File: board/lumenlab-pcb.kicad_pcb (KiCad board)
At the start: 2 copper layers, 72 parts, among them J1 2.1mm Barrel Jack, J2 Screw_Terminal_01x04, J3 Screw_Terminal_01x06, J4 JTAG, SW1 SW_SPST, U1 MP2338, U2 AP7361C-33E, U3 SN74AHCT1G125, U4 SN74HC14DR, U5 ESP32-WROOM-32E, U6 1_Custom_LM386MX-1_NOPB

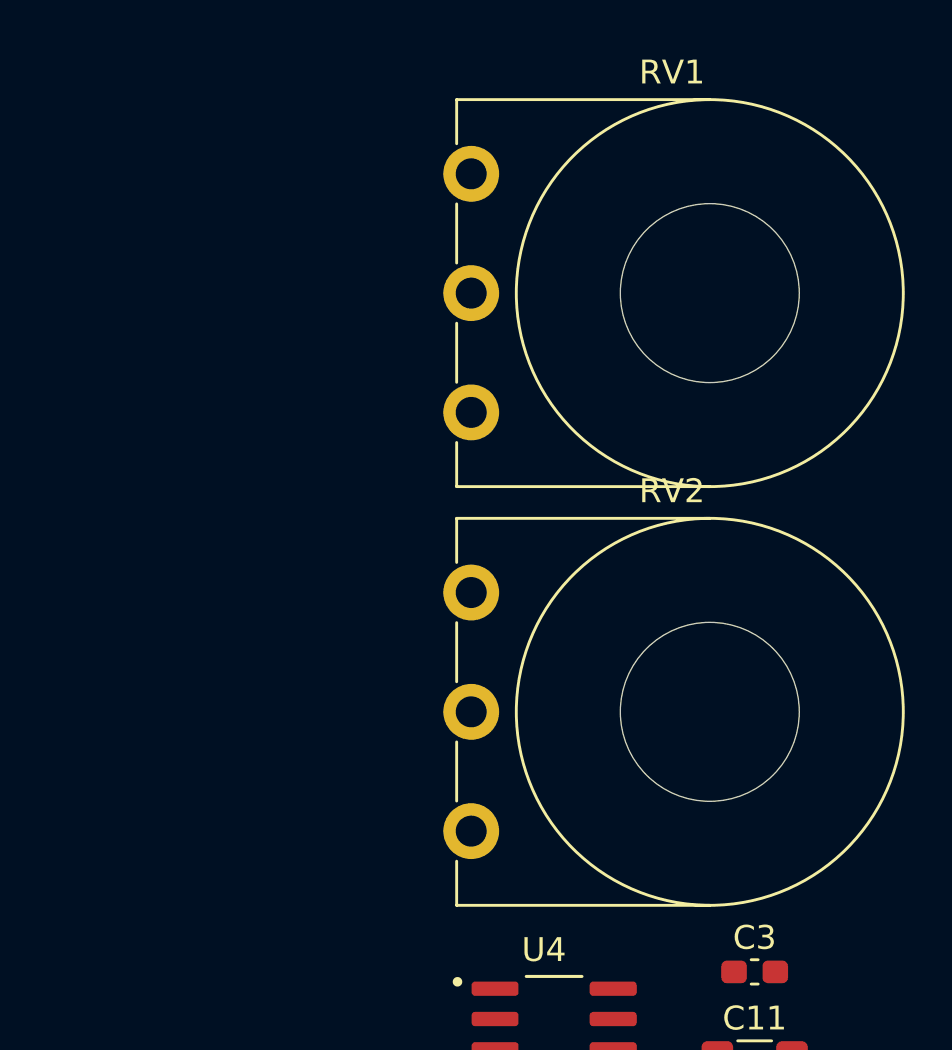
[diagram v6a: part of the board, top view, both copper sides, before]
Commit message: Footprint changes for package sizes and BOM additions
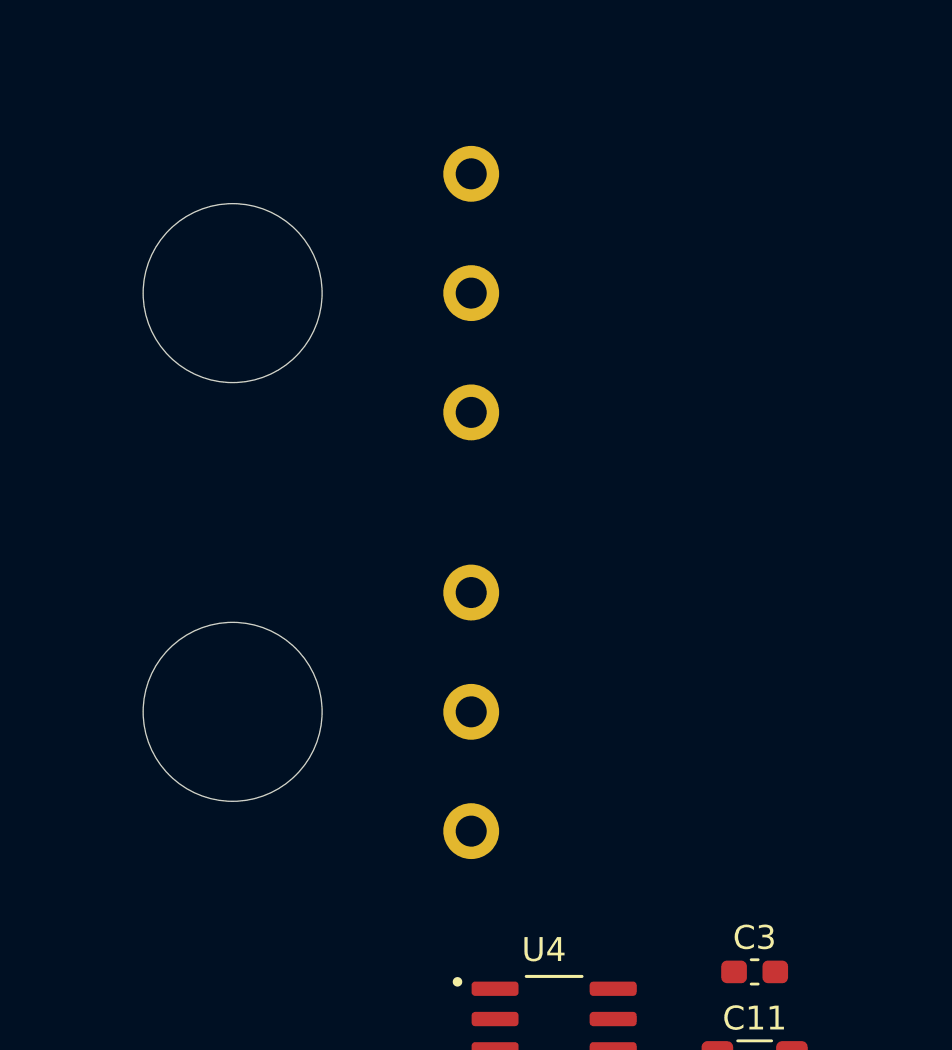
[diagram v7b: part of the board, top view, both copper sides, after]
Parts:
- RV1, RV2: moved to B.Cu
- U6: value 1_Custom_LM386MX-1_NOPB -> LM386MX
- turned RV1 to 180 degrees
- turned RV2 to 180 degrees

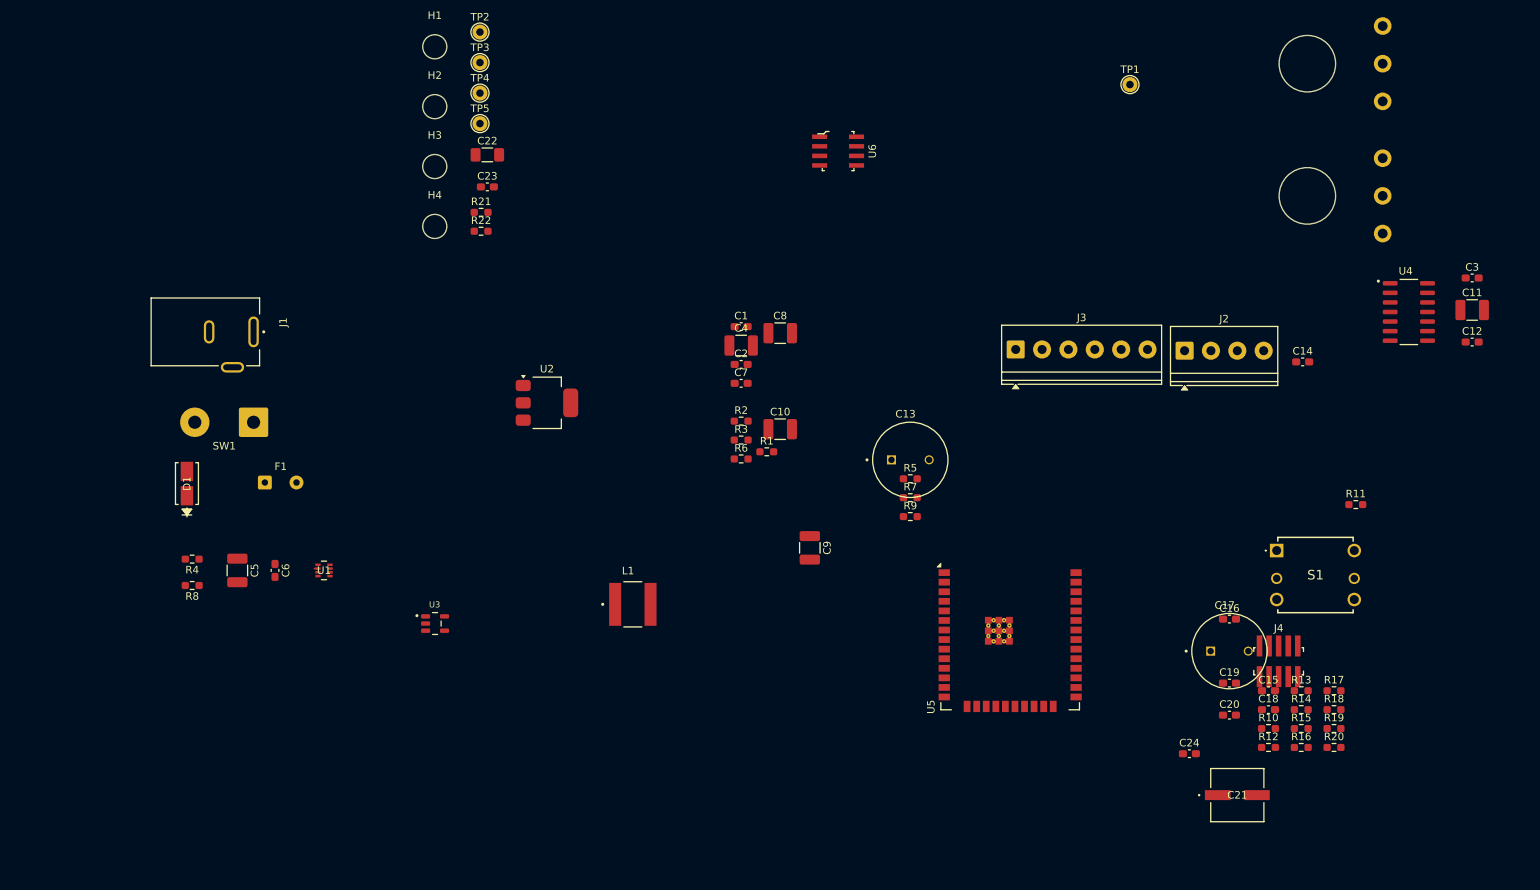
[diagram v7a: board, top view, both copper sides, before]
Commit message: Finalize schematic, footprint assignments, DigiKey BOM
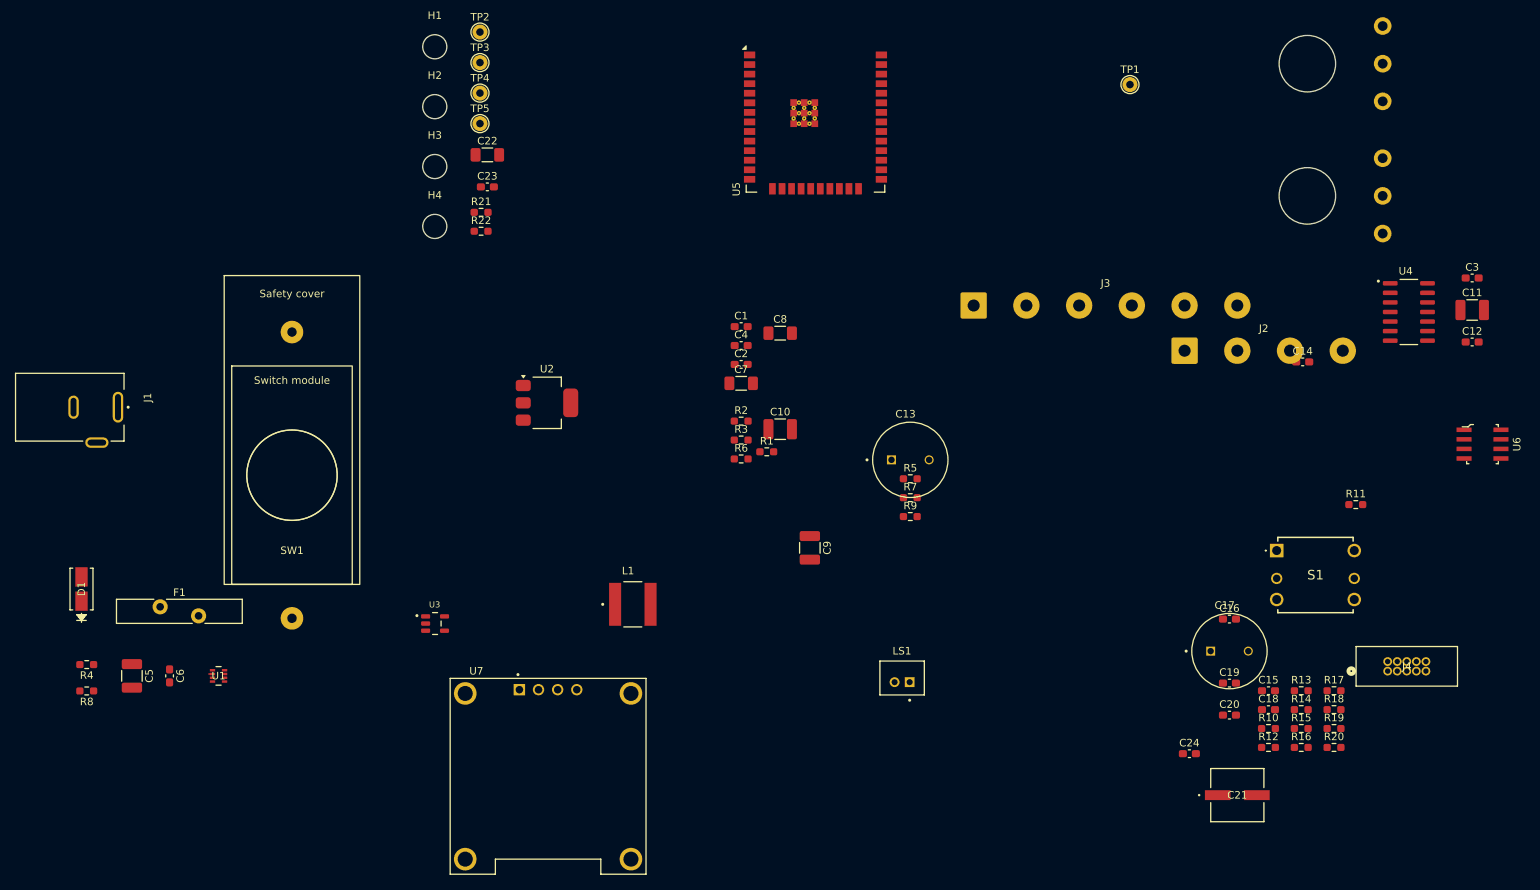
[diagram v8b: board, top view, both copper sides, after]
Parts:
- added LS1: Speaker, 2_Custom_JST-AudioSpeaker:JST_B2B-PH-K-S, F.Cu at (154.0, 129.9)
- added U7: SSD1306, 2_Custom_SSD1306:SSD1306_OLED_MODULE, F.Cu at (107.0, 143.0)
- C4: footprint Capacitor_SMD:C_1210_3225Metric_Pad1.33x2.70mm_HandSolder -> Capacitor_SMD:C_0603_1608Metric_Pad1.08x0.95mm_HandSolder
- C7: footprint Capacitor_SMD:C_0603_1608Metric_Pad1.08x0.95mm_HandSolder -> Capacitor_SMD:C_1206_3216Metric_Pad1.33x1.80mm_HandSolder
- C8: footprint Capacitor_SMD:C_1210_3225Metric_Pad1.33x2.70mm_HandSolder -> Capacitor_SMD:C_1206_3216Metric_Pad1.33x1.80mm_HandSolder
- F1: footprint Connector_Wire:SolderWire-0.25sqmm_1x02_P4.2mm_D0.65mm_OD1.7mm -> Fuse:Fuse_Bourns_MF-RG1000
- J2: value Screw_Terminal_01x04 -> 01x04; footprint TerminalBlock_Phoenix:TerminalBlock_Phoenix_PT-1,5-4-3.5-H_1x04_P3.50mm_Horizontal -> Connector_Wire:SolderWire-0.75sqmm_1x04_P7mm_D1.25mm_OD3.5mm
- J3: value Screw_Terminal_01x06 -> 01x06; footprint TerminalBlock_Phoenix:TerminalBlock_Phoenix_PT-1,5-6-3.5-H_1x06_P3.50mm_Horizontal -> Connector_Wire:SolderWire-0.75sqmm_1x06_P7mm_D1.25mm_OD3.5mm
- J4: footprint digikey-footprints:PinHeader_2x5_P1.27_SMD -> 2_Vendor_JTAG_Header:JTAG-header
- SW1: footprint Connector_Wire:SolderWire-1sqmm_1x02_P7.8mm_D1.4mm_OD3.9mm -> 2_Custom_PowerSwitch:PowerSwitch
- moved U6 94.0 mm to (231.1, 98.9)
- moved U5 73.4 mm to (142.5, 52.5)
- moved F1 21.6 mm to (55.5, 120.5)
- moved J1 20.6 mm to (44.0, 94.0)
- moved D1 19.8 mm to (45.1, 118.1)
- moved C5 19.8 mm to (51.8, 129.7)
- moved C6 19.8 mm to (56.8, 129.7)
- moved R4 19.8 mm to (45.8, 128.2)
- moved R8 19.8 mm to (45.8, 131.7)
- moved U1 19.8 mm to (63.2, 129.7)
- moved J4 14.5 mm to (218.5, 129.0)
- moved SW1 8.68 mm to (73.0, 103.0), turned to 0 degrees
- moved J3 8.07 mm to (163.5, 80.5)
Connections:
- R2 pad 1: Net-(C1-Pad1) -> /BUCK_FB
- R2 pad 2: /BUCK_FB -> Net-(C1-Pad1)
- R21 pad 1: /ESP32_GPIO34 -> Net-(R21-Pad1)
- R21 pad 2: Net-(R21-Pad2) -> /ESP32_GPIO34
- R6 pad 1: /LED_DIN -> Net-(U3-Y)
- R6 pad 2: Net-(U3-Y) -> /LED_DIN
- RV2 pad 2: Net-(R21-Pad2) -> Net-(R21-Pad1)
